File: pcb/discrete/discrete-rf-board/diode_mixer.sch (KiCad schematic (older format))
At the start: 17 parts

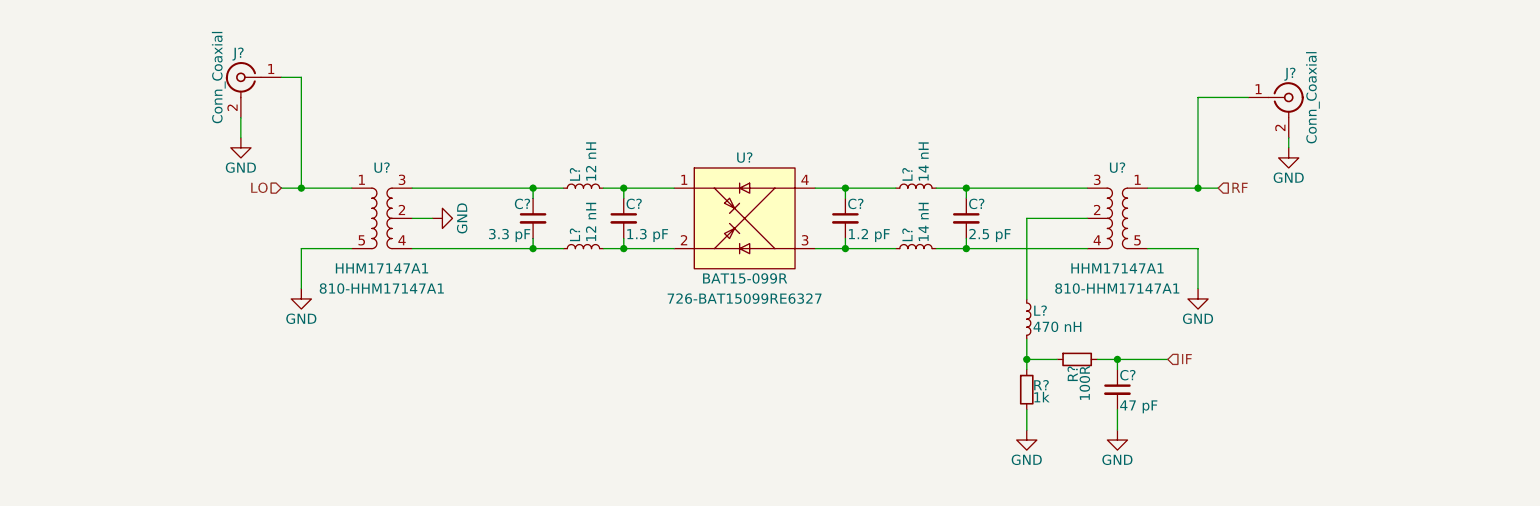
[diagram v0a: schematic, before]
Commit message: Capture IF amplifier stages and work on LNA stages
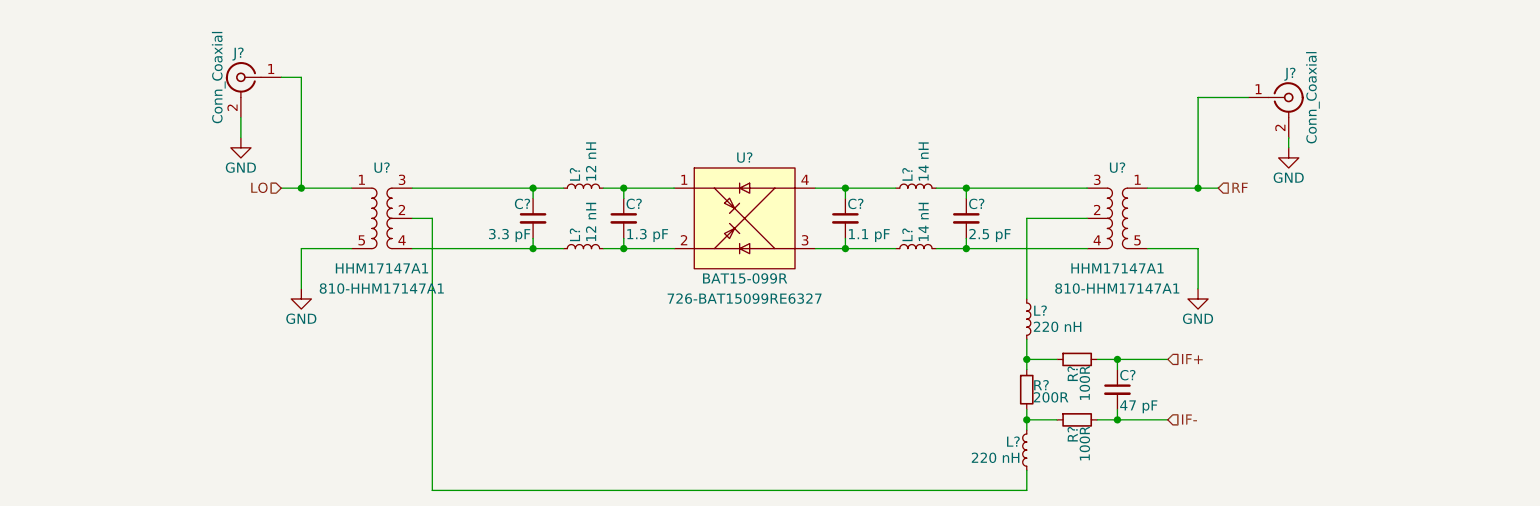
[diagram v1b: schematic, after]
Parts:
- added L?: 220 nH, symbol Device:L_Small
- added R?: 100R, symbol Device:R_Small
- C?: value 1.2 pF -> 1.1 pF
- L?: value 470 nH -> 220 nH
- R?: value 1k -> 200R
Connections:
- net GND: no longer C?.2, R?.2, U?.2 (COMMON)
- net IF renamed IF+
- new net: L?.2, U?.2 (COMMON)
- new net: L?.1, R?.1, R?.2
- new net IF-: C?.2, R?.2
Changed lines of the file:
@@
 $Descr A4 11693 8268
 encoding utf-8
-Sheet 4 8
+Sheet 3 9
 Title ""
 Date ""
@@
 AR Path="/5CA6B0AA/5CC4015A/5CC1F89D" Ref="C?"  Part="1"
 F 0 "C?" H 6410 3670 50  0000 L CNN
-F 1 "1.2 pF" H 6410 3520 50  0000 L CNN
+F 1 "1.1 pF" H 6410 3520 50  0000 L CNN
 F 2 "" H 6400 3600 50  0001 C CNN
 F 3 "~" H 6400 3600 50  0001 C CNN
@@
 	1    0    0    -1
 $EndComp
-$Comp
-L power:GND #PWR?
-U 1 1 5CC2742C
-P 4350 3600
-AR Path="/5CA6B0AA/5CC1CC09/5CC2742C" Ref="#PWR?"  Part="1"
-AR Path="/5CA6B0AA/5CC4015A/5CC2742C" Ref="#PWR?"  Part="1"
-F 0 "#PWR?" H 4350 3350 50  0001 C CNN
-F 1 "GND" H 4350 3450 50  0000 C CNN
-F 2 "" H 4350 3600 50  0001 C CNN
-F 3 "" H 4350 3600 50  0001 C CNN
-	1    4350 3600
-	0    -1   -1   0
-$EndComp
 Wire Wire Line
 	4250 3450 4850 3450
@@
 AR Path="/5CA6B0AA/5CC4015A/5CC289D9" Ref="L?"  Part="1"
 F 0 "L?" H 7330 4140 50  0000 L CNN
-F 1 "470 nH" H 7330 4060 50  0000 L CNN
+F 1 "220 nH" H 7330 4060 50  0000 L CNN
 F 2 "" H 7300 4100 50  0001 C CNN
 F 3 "~" H 7300 4100 50  0001 C CNN
@@
 AR Path="/5CA6B0AA/5CC4015A/5CC29B4E" Ref="R?"  Part="1"
 F 0 "R?" H 7330 4470 50  0000 L CNN
-F 1 "1k" H 7330 4410 50  0000 L CNN
+F 1 "200R" H 7330 4410 50  0000 L CNN
 F 2 "" H 7300 4450 50  0001 C CNN
 F 3 "~" H 7300 4450 50  0001 C CNN
@@
 $EndComp
 $Comp
-L power:GND #PWR?
-U 1 1 5CC2A5B0
-P 7300 4650
-AR Path="/5CA6B0AA/5CC1CC09/5CC2A5B0" Ref="#PWR?"  Part="1"
-AR Path="/5CA6B0AA/5CC4015A/5CC2A5B0" Ref="#PWR?"  Part="1"
-F 0 "#PWR?" H 7300 4400 50  0001 C CNN
-F 1 "GND" H 7300 4500 50  0000 C CNN
-F 2 "" H 7300 4650 50  0001 C CNN
-F 3 "" H 7300 4650 50  0001 C CNN
-	1    7300 4650
-	1    0    0    -1
-$EndComp
-$Comp
-L power:GND #PWR?
-U 1 1 5CC2A9CD
-P 7750 4650
-AR Path="/5CA6B0AA/5CC1CC09/5CC2A9CD" Ref="#PWR?"  Part="1"
-AR Path="/5CA6B0AA/5CC4015A/5CC2A9CD" Ref="#PWR?"  Part="1"
-F 0 "#PWR?" H 7750 4400 50  0001 C CNN
-F 1 "GND" H 7750 4500 50  0000 C CNN
-F 2 "" H 7750 4650 50  0001 C CNN
-F 3 "" H 7750 4650 50  0001 C CNN
-	1    7750 4650
-	1    0    0    -1
-$EndComp
-$Comp
 L Device:C_Small C?
 U 1 1 5CC2B0AC
@@
 	7300 4200 7300 4300
 Wire Wire Line
-	7300 4550 7300 4650
-Wire Wire Line
 	7450 4300 7300 4300
 Connection ~ 7300 4300
@@
 Wire Wire Line
 	7750 4300 7750 4350
-Wire Wire Line
-	7750 4550 7750 4650
 $Comp
 L power:GND #PWR?
@@
 Text HLabel 8250 3450 2    50   Input ~ 0
 RF
-Text HLabel 8000 4300 2    50   Input ~ 0
-IF
 Wire Wire Line
 	8000 4300 7750 4300
 Connection ~ 7750 4300
+Wire Wire Line
+	4350 3600 4350 4950
+Wire Wire Line
+	4350 4950 7300 4950
+$Comp
+L Device:L_Small L?
+U 1 1 5CC5AE0B
+P 7300 4750
+AR Path="/5CA6B0AA/5CC1CC09/5CC5AE0B" Ref="L?"  Part="1"
+AR Path="/5CA6B0AA/5CC4015A/5CC5AE0B" Ref="L?"  Part="1"
+F 0 "L?" H 7330 4790 50  0000 L CNN
+F 1 "220 nH" H 7330 4710 50  0000 L CNN
+F 2 "" H 7300 4750 50  0001 C CNN
+F 3 "~" H 7300 4750 50  0001 C CNN
+	1    7300 4750
+	-1   0    0    -1
+$EndComp
+Wire Wire Line
+	7300 4850 7300 4950
+Wire Wire Line
+	7300 4650 7300 4600
+$Comp
+L Device:R_Small R?
+U 1 1 5CC5DD55
+P 7550 4600
+AR Path="/5CA6B0AA/5CC1CC09/5CC5DD55" Ref="R?"  Part="1"
+AR Path="/5CA6B0AA/5CC4015A/5CC5DD55" Ref="R?"  Part="1"
+F 0 "R?" H 7580 4620 50  0000 L CNN
+F 1 "100R" H 7580 4560 50  0000 L CNN
+F 2 "" H 7550 4600 50  0001 C CNN
+F 3 "~" H 7550 4600 50  0001 C CNN
+	1    7550 4600
+	0    -1   1    0
+$EndComp
+Wire Wire Line
+	7450 4600 7300 4600
+Connection ~ 7300 4600
+Wire Wire Line
+	7300 4600 7300 4550
+Wire Wire Line
+	7650 4600 7750 4600
+Wire Wire Line
+	7750 4600 7750 4550
+Wire Wire Line
+	8000 4600 7750 4600
+Connection ~ 7750 4600
+Text HLabel 8000 4300 2    50   Input ~ 0
+IF+
+Text HLabel 8000 4600 2    50   Input ~ 0
+IF-
 $EndSCHEMATC

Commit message: Save changes while moving over to the new laptop
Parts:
- gave numbers to parts that had none: 19

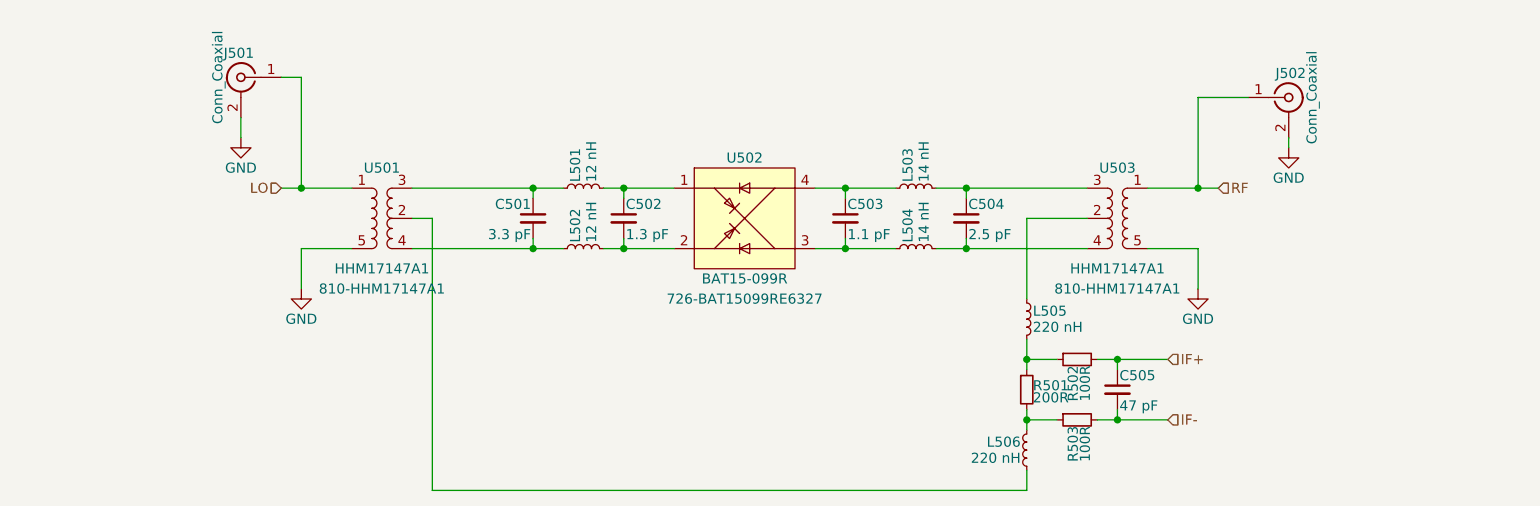
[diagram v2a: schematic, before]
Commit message: Work on LNA staging, attenuator design, various fixes elsewhere
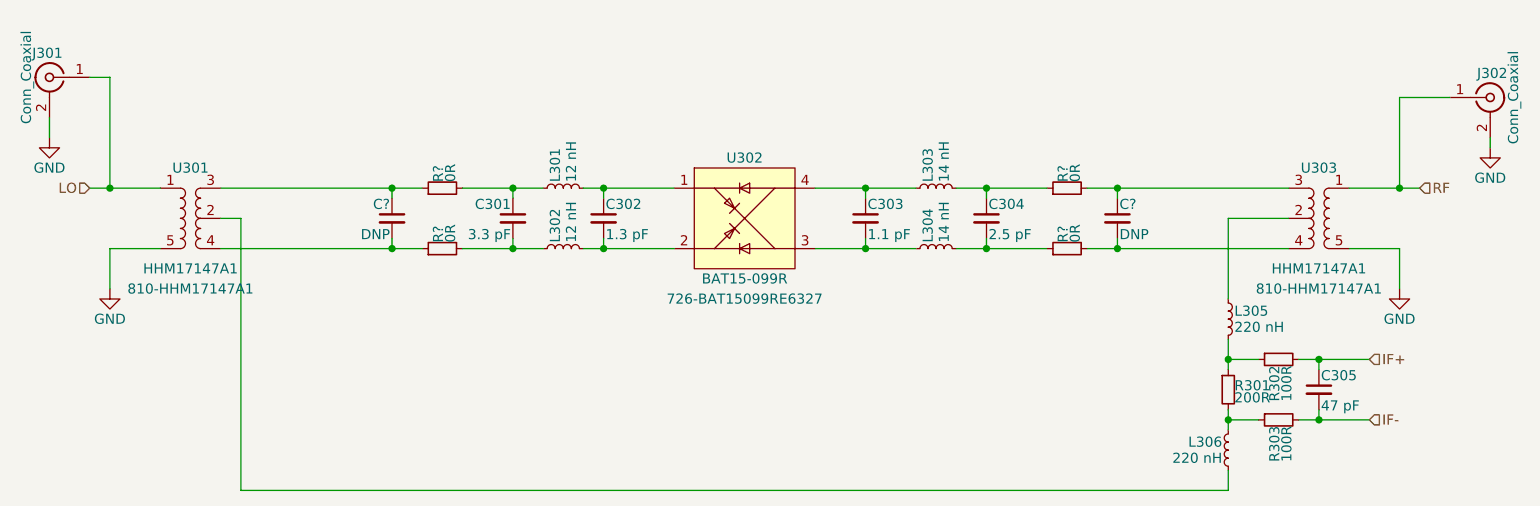
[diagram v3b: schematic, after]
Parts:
- added C? (x2): DNP, symbol Device:C_Small
- added R? (x4): 0R, symbol Device:R_Small
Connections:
- net at C301.1, L301.1: now also R?.2; no longer U301.3 (+)
- net at C301.2, L302.1: now also R?.2; no longer U301.4 (-)
- net at C304.1, L303.2: now also R?.1; no longer U303.3 (+)
- net at C304.2, L304.2: now also R?.1; no longer U303.4 (-)
- new net: C?.1, R?.1, U301.3 (+)
- new net: C?.2, R?.1, U301.4 (-)
- new net: C?.1, R?.2, U303.3 (+)
- new net: C?.2, R?.2, U303.4 (-)
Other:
- moved on the sheet: C301, C302, C303, C304, C305, J301, J302, L301, L302, L303, L304, L305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

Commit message: Merge stuff I guess, hopefully this doesn't break too much
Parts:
- removed U301, U303: HHM17147A1, symbol discrete-parts:HHM17147A1
- added T? (x2): HHM17147A1, symbol discrete-parts:HHM17147A1
- gave numbers to parts that had none: 6
- renumbered C301 to C302, C302 to C303, C303 to C304, C304 to C305, C305 to C307, R301 to R305, R302 to R306, R303 to R307
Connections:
- net GND: now also T?.5 (GND), T?.5 (GND)
- net LO: now also T?.1 (SINGLE)
- net RF: now also T?.1 (SINGLE)
- net at L306.2: now also T?.2 (COMMON)
- net at C301.1, R301.1: now also T?.3 (+)
- net at C301.2, R302.1: now also T?.4 (-)
- net at L305.1: now also T?.2 (COMMON)
- net at C306.1, R303.2: now also T?.3 (+)
- net at C306.2, R304.2: now also T?.4 (-)
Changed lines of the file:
@@
 $EndComp
 $Comp
-L Device:C_Small C303
+L Device:C_Small C304
 U 1 1 5CC1F89D
 P 6500 3600
-AR Path="/5CA6B0AA/5CC1CC09/5CC1F89D" Ref="C303"  Part="1"
-AR Path="/5CA6B0AA/5CC4015A/5CC1F89D" Ref="C503"  Part="1"
-F 0 "C303" H 6510 3670 50  0000 L CNN
+AR Path="/5CA6B0AA/5CC1CC09/5CC1F89D" Ref="C304"  Part="1"
+AR Path="/5CA6B0AA/5CC4015A/5CC1F89D" Ref="C504"  Part="1"
+F 0 "C304" H 6510 3670 50  0000 L CNN
 F 1 "1.1 pF" H 6510 3520 50  0000 L CNN
 F 2 "" H 6500 3600 50  0001 C CNN
@@
 $EndComp
 $Comp
-L Device:C_Small C304
+L Device:C_Small C305
 U 1 1 5CC20238
 P 7100 3600
-AR Path="/5CA6B0AA/5CC1CC09/5CC20238" Ref="C304"  Part="1"
-AR Path="/5CA6B0AA/5CC4015A/5CC20238" Ref="C504"  Part="1"
-F 0 "C304" H 7110 3670 50  0000 L CNN
+AR Path="/5CA6B0AA/5CC1CC09/5CC20238" Ref="C305"  Part="1"
+AR Path="/5CA6B0AA/5CC4015A/5CC20238" Ref="C505"  Part="1"
+F 0 "C305" H 7110 3670 50  0000 L CNN
 F 1 "2.5 pF" H 7110 3520 50  0000 L CNN
 F 2 "" H 7100 3600 50  0001 C CNN
@@
 Wire Wire Line
 	7100 3750 7100 3700
-$Comp
-L discrete-parts:HHM17147A1 U301
-U 1 1 5CC2572D
-P 3150 3600
-AR Path="/5CA6B0AA/5CC1CC09/5CC2572D" Ref="U301"  Part="1"
-AR Path="/5CA6B0AA/5CC4015A/5CC2572D" Ref="U501"  Part="1"
-F 0 "U301" H 3150 3850 50  0000 C CNN
-F 1 "HHM17147A1" H 3150 3350 50  0000 C CNN
-F 2 "" H 3150 3850 50  0001 C CNN
-F 3 "" H 3150 3850 50  0001 C CNN
-F 4 "810-HHM17147A1" H 3150 3250 50  0000 C CNN "Mouser"
-	1    3150 3600
-	-1   0    0    -1
-$EndComp
-$Comp
-L discrete-parts:HHM17147A1 U303
-U 1 1 5CC264D0
-P 8750 3600
-AR Path="/5CA6B0AA/5CC1CC09/5CC264D0" Ref="U303"  Part="1"
-AR Path="/5CA6B0AA/5CC4015A/5CC264D0" Ref="U503"  Part="1"
-F 0 "U303" H 8750 3850 50  0000 C CNN
-F 1 "HHM17147A1" H 8750 3350 50  0000 C CNN
-F 2 "" H 8750 3850 50  0001 C CNN
-F 3 "" H 8750 3850 50  0001 C CNN
-F 4 "810-HHM17147A1" H 8750 3250 50  0000 C CNN "Mouser"
-	1    8750 3600
-	1    0    0    -1
-$EndComp
 Wire Wire Line
 	3300 3600 3400 3600
@@
 	8300 3600 8300 4000
 $Comp
-L Device:R_Small R301
+L Device:R_Small R305
 U 1 1 5CC29B4E
 P 8300 4450
-AR Path="/5CA6B0AA/5CC1CC09/5CC29B4E" Ref="R301"  Part="1"
-AR Path="/5CA6B0AA/5CC4015A/5CC29B4E" Ref="R501"  Part="1"
-F 0 "R301" H 8330 4470 50  0000 L CNN
+AR Path="/5CA6B0AA/5CC1CC09/5CC29B4E" Ref="R305"  Part="1"
+AR Path="/5CA6B0AA/5CC4015A/5CC29B4E" Ref="R505"  Part="1"
+F 0 "R305" H 8330 4470 50  0000 L CNN
 F 1 "200R" H 8330 4410 50  0000 L CNN
 F 2 "" H 8300 4450 50  0001 C CNN
@@
 $EndComp
 $Comp
-L Device:R_Small R302
+L Device:R_Small R306
 U 1 1 5CC29F9D
 P 8550 4300
-AR Path="/5CA6B0AA/5CC1CC09/5CC29F9D" Ref="R302"  Part="1"
-AR Path="/5CA6B0AA/5CC4015A/5CC29F9D" Ref="R502"  Part="1"
-F 0 "R302" H 8580 4320 50  0000 L CNN
+AR Path="/5CA6B0AA/5CC1CC09/5CC29F9D" Ref="R306"  Part="1"
+AR Path="/5CA6B0AA/5CC4015A/5CC29F9D" Ref="R506"  Part="1"
+F 0 "R306" H 8580 4320 50  0000 L CNN
 F 1 "100R" H 8580 4260 50  0000 L CNN
 F 2 "" H 8550 4300 50  0001 C CNN
@@
 $EndComp
 $Comp
-L Device:C_Small C305
+L Device:C_Small C307
 U 1 1 5CC2B0AC
 P 8750 4450
-AR Path="/5CA6B0AA/5CC1CC09/5CC2B0AC" Ref="C305"  Part="1"
-AR Path="/5CA6B0AA/5CC4015A/5CC2B0AC" Ref="C505"  Part="1"
-F 0 "C305" H 8760 4520 50  0000 L CNN
+AR Path="/5CA6B0AA/5CC1CC09/5CC2B0AC" Ref="C307"  Part="1"
+AR Path="/5CA6B0AA/5CC4015A/5CC2B0AC" Ref="C507"  Part="1"
+F 0 "C307" H 8760 4520 50  0000 L CNN
 F 1 "47 pF" H 8760 4370 50  0000 L CNN
 F 2 "" H 8750 4450 50  0001 C CNN
@@
 	8300 4650 8300 4600
 $Comp
-L Device:R_Small R303
+L Device:R_Small R307
 U 1 1 5CC5DD55
 P 8550 4600
-AR Path="/5CA6B0AA/5CC1CC09/5CC5DD55" Ref="R303"  Part="1"
-AR Path="/5CA6B0AA/5CC4015A/5CC5DD55" Ref="R503"  Part="1"
-F 0 "R303" H 8580 4620 50  0000 L CNN
+AR Path="/5CA6B0AA/5CC1CC09/5CC5DD55" Ref="R307"  Part="1"
+AR Path="/5CA6B0AA/5CC4015A/5CC5DD55" Ref="R507"  Part="1"
+F 0 "R307" H 8580 4620 50  0000 L CNN
 F 1 "100R" H 8580 4560 50  0000 L CNN
 F 2 "" H 8550 4600 50  0001 C CNN
@@
 $EndComp
 $Comp
-L Device:C_Small C301
+L Device:C_Small C302
 U 1 1 5CC1F7BA
 P 4750 3600
-AR Path="/5CA6B0AA/5CC1CC09/5CC1F7BA" Ref="C301"  Part="1"
-AR Path="/5CA6B0AA/5CC4015A/5CC1F7BA" Ref="C501"  Part="1"
-F 0 "C301" H 4760 3670 50  0000 L CNN
+AR Path="/5CA6B0AA/5CC1CC09/5CC1F7BA" Ref="C302"  Part="1"
+AR Path="/5CA6B0AA/5CC4015A/5CC1F7BA" Ref="C502"  Part="1"
+F 0 "C302" H 4760 3670 50  0000 L CNN
 F 1 "3.3 pF" H 4760 3520 50  0000 L CNN
 F 2 "" H 4750 3600 50  0001 C CNN
@@
 $EndComp
 $Comp
-L Device:C_Small C302
+L Device:C_Small C303
 U 1 1 5CC1E94D
 P 5200 3600
-AR Path="/5CA6B0AA/5CC1CC09/5CC1E94D" Ref="C302"  Part="1"
-AR Path="/5CA6B0AA/5CC4015A/5CC1E94D" Ref="C502"  Part="1"
-F 0 "C302" H 5210 3670 50  0000 L CNN
+AR Path="/5CA6B0AA/5CC1CC09/5CC1E94D" Ref="C303"  Part="1"
+AR Path="/5CA6B0AA/5CC4015A/5CC1E94D" Ref="C503"  Part="1"
+F 0 "C303" H 5210 3670 50  0000 L CNN
 F 1 "1.3 pF" H 5210 3520 50  0000 L CNN
 F 2 "" H 5200 3600 50  0001 C CNN
@@
 	5200 3750 5550 3750
 $Comp
-L Device:C_Small C?
+L Device:C_Small C301
 U 1 1 5D51EF09
 P 4150 3600
-AR Path="/5CA6B0AA/5CC1CC09/5D51EF09" Ref="C?"  Part="1"
-AR Path="/5CA6B0AA/5CC4015A/5D51EF09" Ref="C?"  Part="1"
-F 0 "C?" H 4160 3670 50  0000 L CNN
+AR Path="/5CA6B0AA/5CC1CC09/5D51EF09" Ref="C301"  Part="1"
+AR Path="/5CA6B0AA/5CC4015A/5D51EF09" Ref="C501"  Part="1"
+F 0 "C301" H 4160 3670 50  0000 L CNN
 F 1 "DNP" H 4160 3520 50  0000 L CNN
 F 2 "" H 4150 3600 50  0001 C CNN
@@
 $EndComp
 $Comp
-L Device:R_Small R?
+L Device:R_Small R301
 U 1 1 5D51FC82
 P 4400 3450
-F 0 "R?" H 4430 3470 50  0000 L CNN
+AR Path="/5CA6B0AA/5CC1CC09/5D51FC82" Ref="R301"  Part="1"
+AR Path="/5CA6B0AA/5CC4015A/5D51FC82" Ref="R501"  Part="1"
+F 0 "R301" H 4430 3470 50  0000 L CNN
 F 1 "0R" H 4430 3410 50  0000 L CNN
 F 2 "" H 4400 3450 50  0001 C CNN
@@
 $EndComp
 $Comp
-L Device:R_Small R?
+L Device:R_Small R302
 U 1 1 5D5221DB
 P 4400 3750
-F 0 "R?" H 4430 3770 50  0000 L CNN
+AR Path="/5CA6B0AA/5CC1CC09/5D5221DB" Ref="R302"  Part="1"
+AR Path="/5CA6B0AA/5CC4015A/5D5221DB" Ref="R502"  Part="1"
+F 0 "R302" H 4430 3770 50  0000 L CNN
 F 1 "0R" H 4430 3710 50  0000 L CNN
 F 2 "" H 4400 3750 50  0001 C CNN
@@
 	4150 3750 4300 3750
 $Comp
-L Device:C_Small C?
+L Device:C_Small C306
 U 1 1 5D52D7BD
 P 7750 3600
-AR Path="/5CA6B0AA/5CC1CC09/5D52D7BD" Ref="C?"  Part="1"
-AR Path="/5CA6B0AA/5CC4015A/5D52D7BD" Ref="C?"  Part="1"
-F 0 "C?" H 7760 3670 50  0000 L CNN
+AR Path="/5CA6B0AA/5CC1CC09/5D52D7BD" Ref="C306"  Part="1"
+AR Path="/5CA6B0AA/5CC4015A/5D52D7BD" Ref="C506"  Part="1"
+F 0 "C306" H 7760 3670 50  0000 L CNN
 F 1 "DNP" H 7760 3520 50  0000 L CNN
 F 2 "" H 7750 3600 50  0001 C CNN
@@
 $EndComp
 $Comp
-L Device:R_Small R?
+L Device:R_Small R303
 U 1 1 5D52D7C3
 P 7500 3450
-F 0 "R?" H 7530 3470 50  0000 L CNN
+AR Path="/5CA6B0AA/5CC1CC09/5D52D7C3" Ref="R303"  Part="1"
+AR Path="/5CA6B0AA/5CC4015A/5D52D7C3" Ref="R503"  Part="1"
+F 0 "R303" H 7530 3470 50  0000 L CNN
 F 1 "0R" H 7530 3410 50  0000 L CNN
 F 2 "" H 7500 3450 50  0001 C CNN
@@
 $EndComp
 $Comp
-L Device:R_Small R?
+L Device:R_Small R304
 U 1 1 5D52D7C9
 P 7500 3750
-F 0 "R?" H 7530 3770 50  0000 L CNN
+AR Path="/5CA6B0AA/5CC1CC09/5D52D7C9" Ref="R304"  Part="1"
+AR Path="/5CA6B0AA/5CC4015A/5D52D7C9" Ref="R504"  Part="1"
+F 0 "R304" H 7530 3770 50  0000 L CNN
 F 1 "0R" H 7530 3710 50  0000 L CNN
 F 2 "" H 7500 3750 50  0001 C CNN
@@
 Wire Wire Line
 	3400 4950 8300 4950
+$Comp
+L discrete-parts:HHM17147A1 T?
+U 1 1 5D1B92FB
+P 3150 3600
+AR Path="/5CA6B0AA/5CC1CC09/5D1B92FB" Ref="T?"  Part="1"
+AR Path="/5CA6B0AA/5CC4015A/5D1B92FB" Ref="T?"  Part="1"
+F 0 "T?" H 3150 3850 50  0000 C CNN
+F 1 "HHM17147A1" H 3150 3350 50  0000 C CNN
+F 2 "" H 3150 3850 50  0001 C CNN
+F 3 "" H 3150 3850 50  0001 C CNN
+F 4 "810-HHM17147A1" H 3150 3250 50  0000 C CNN "Mouser"
+	1    3150 3600
+	-1   0    0    -1
+$EndComp
+$Comp
+L discrete-parts:HHM17147A1 T?
+U 1 1 5D1C03F7
+P 8750 3600
+AR Path="/5CA6B0AA/5CC1CC09/5D1C03F7" Ref="T?"  Part="1"
+AR Path="/5CA6B0AA/5CC4015A/5D1C03F7" Ref="T?"  Part="1"
+F 0 "T?" H 8750 3850 50  0000 C CNN
+F 1 "HHM17147A1" H 8750 3350 50  0000 C CNN
+F 2 "" H 8750 3850 50  0001 C CNN
+F 3 "" H 8750 3850 50  0001 C CNN
+F 4 "810-HHM17147A1" H 8750 3250 50  0000 C CNN "Mouser"
+	1    8750 3600
+	1    0    0    -1
+$EndComp
 $EndSCHEMATC
